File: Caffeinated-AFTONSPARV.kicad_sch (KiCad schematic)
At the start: 35 parts, among them J1 PWR, J2 LED, J3 TagConnect, J4 USB, Q1 AO3400A, Q2 AO3400A, Q3 AO3400A, SW1 SW_Push, U1 ESP32-C3-MINI-1-[H/N]4, U2 SY8201ABC

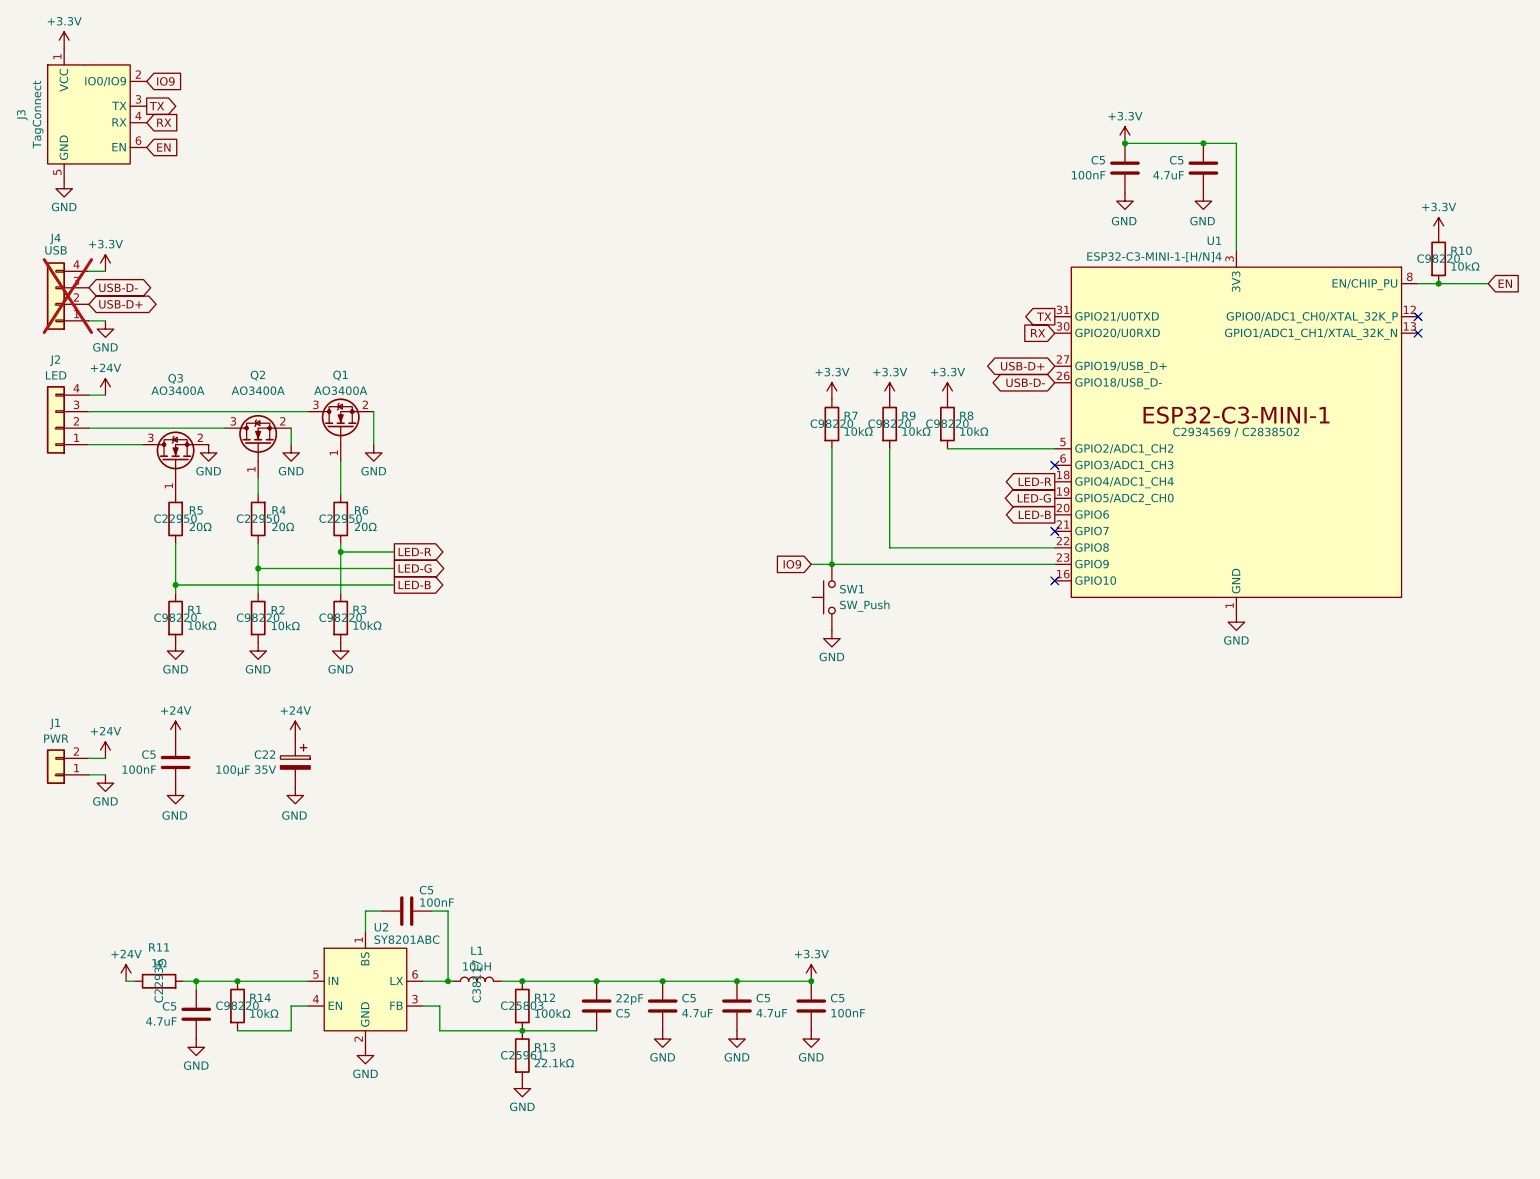
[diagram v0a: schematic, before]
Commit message: optimize bom for jlcpcb basic parts
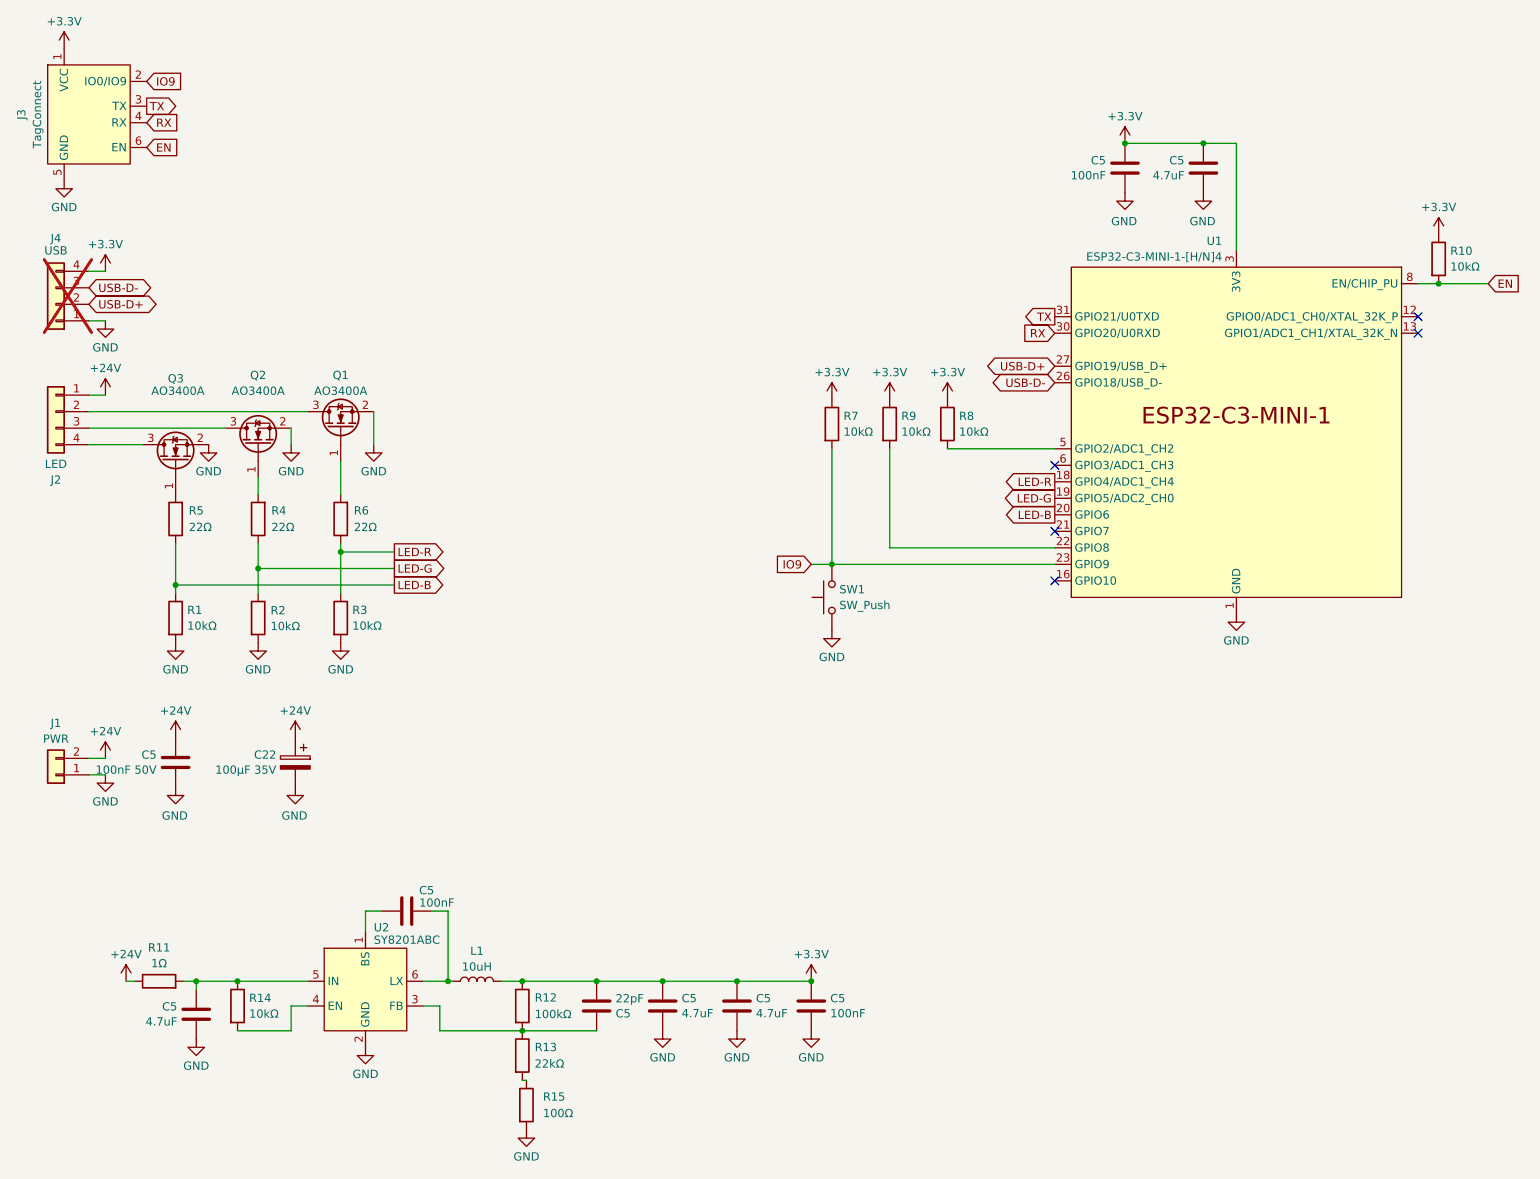
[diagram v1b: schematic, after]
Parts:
- added R15: 100Ω, Resistor_SMD:R_0402_1005Metric, symbol Device:R
- C22: LCSC C2831717 -> (none)
- C5: footprint Capacitor_SMD:C_0603_1608Metric -> Capacitor_SMD:C_0402_1005Metric; LCSC C14663 -> (none)
- C5: footprint Capacitor_SMD:C_0805_2012Metric -> Capacitor_SMD:C_1206_3216Metric; LCSC C560882 -> (none)
- C5: footprint Capacitor_SMD:C_0603_1608Metric -> Capacitor_SMD:C_0402_1005Metric; LCSC C105620 -> (none)
- C5: value 100nF -> 100nF 50V; footprint Capacitor_SMD:C_0603_1608Metric -> Capacitor_SMD:C_0402_1005Metric; LCSC C14663 -> (none)
- J1, J2, J3, J4: LCSC - -> (none)
- L1: LCSC C38117 -> (none)
- Q1, Q2, Q3: LCSC C347475 -> (none)
- R1, R10, R14, R2, R3, R7, R8, R9: footprint Resistor_SMD:R_0603_1608Metric -> Resistor_SMD:R_0402_1005Metric; LCSC C98220 -> (none)
- R11: LCSC C22936 -> (none)
- R12: footprint Resistor_SMD:R_0603_1608Metric -> Resistor_SMD:R_0402_1005Metric; LCSC C25803 -> (none)
- R13: value 22.1kΩ -> 22kΩ; footprint Resistor_SMD:R_0603_1608Metric -> Resistor_SMD:R_0402_1005Metric; LCSC C25961 -> (none)
- R4, R5, R6: value 20Ω -> 22Ω; footprint Resistor_SMD:R_0603_1608Metric -> Resistor_SMD:R_0402_1005Metric; LCSC C22950 -> (none)
- SW1: LCSC C2910748 -> (none)
- U1: LCSC C2934569 / C2838502 -> (none)
- U2: LCSC C108052 -> (none)
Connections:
- net +24V: now also J2.1 (Pin_1); no longer J2.4 (Pin_4)
- net GND: now also R15.2; no longer R13.2
- net at Q3.3 (D): now also J2.4 (Pin_4); no longer J2.1 (Pin_1)
- net at J2.2 (Pin_2): now also Q1.3 (D); no longer Q2.3 (D)
- net at J2.3 (Pin_3): now also Q2.3 (D); no longer Q1.3 (D)
- new net: R13.2, R15.1
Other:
- moved on the sheet: J2
